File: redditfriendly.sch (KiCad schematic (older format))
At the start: 48 parts, among them J1 PJ-077, J2 Conn_01x06_Female, J3 Conn_01x02_Female, J4 Conn_01x06_Female, J5 Conn_01x04_Female, J6 Conn_01x6_Female, Q1 MMBT2222A-TP, Q2 MMBT2222A-TP, SW1 SW_Push, SW2 SW_Push, U1 ESP32-WROOM-32U, U2 LMR33620Simple, U3 TLC5971

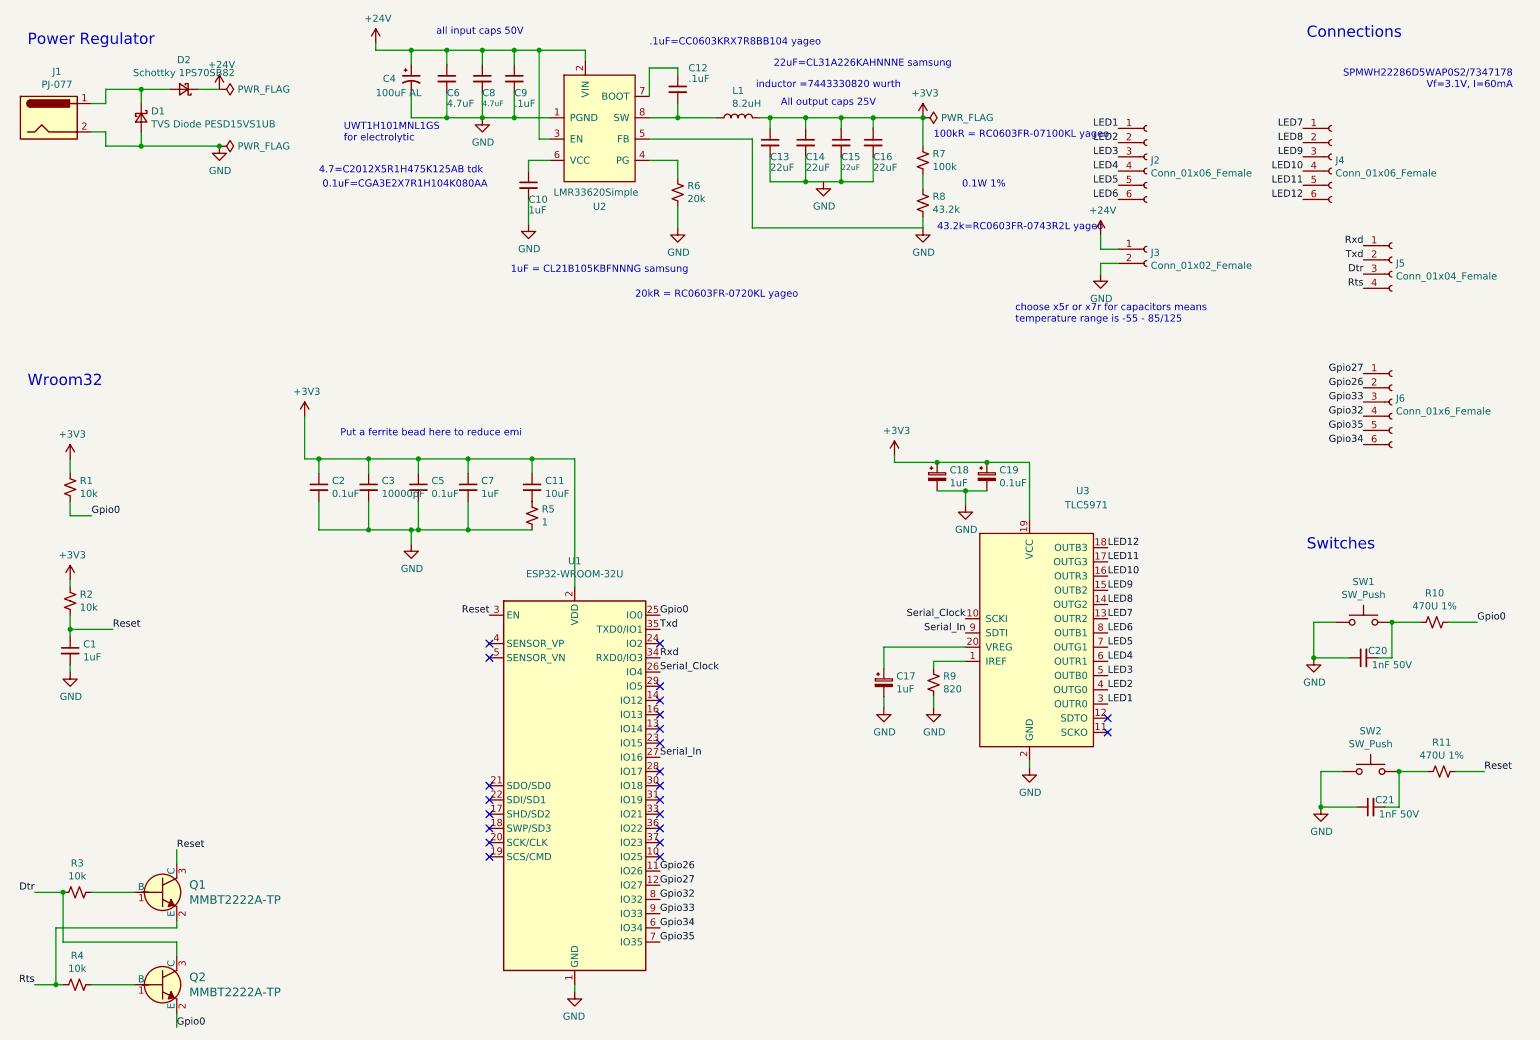
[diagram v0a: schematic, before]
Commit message: Created pmic footprint
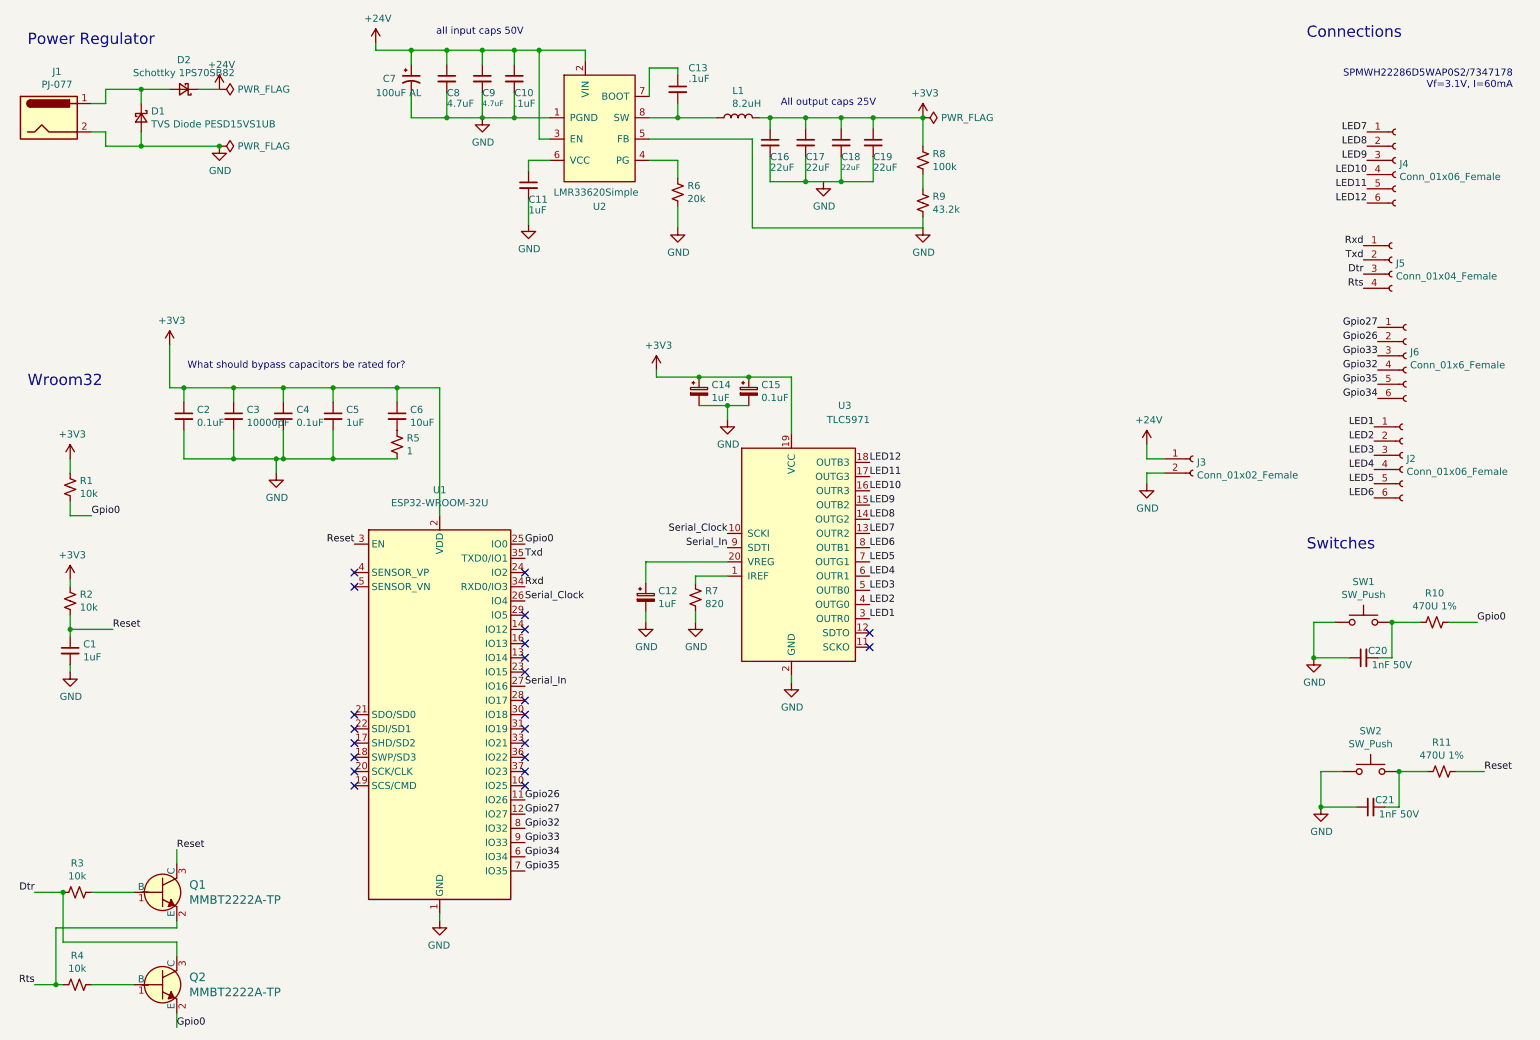
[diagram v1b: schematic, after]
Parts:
- C7: renamed from C4; footprint Capacitor_SMD:CP_Elec_6.3x5.4 -> (none)
- L1: footprint Keith:wurth 7443330820 8.2uH -> keith:Wurth 74437349012 Inductor
- U2: footprint Keith:lmr33620HSOIC -> (none)
- renumbered C9 to C10, C10 to C11, C17 to C12, C12 to C13, C18 to C14, C19 to C15, C13 to C16, C14 to C17, C15 to C18, C16 to C19, C5 to C4, C7 to C5, C11 to C6, C6 to C8, C8 to C9, R9 to R7, R7 to R8, R8 to R9
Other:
- note added: "What should bypass capacitors be rated for?"
- note removed: ".1uF=CC0603KRX7R8BB104 yageo"
- note removed: "0.1W 1%"
- note removed: "0.1uF=CGA3E2X7R1H104K080AA"
- note removed: "100kR = RC0603FR-07100KL yageo"
- note removed: "1uF = CL21B105KBFNNNG samsung"
- note removed: "20kR = RC0603FR-0720KL yageo"
- note removed: "22uF=CL31A226KAHNNNE samsung"
- note removed: "4.7=C2012X5R1H475K125AB tdk"
- note removed: "43.2k=RC0603FR-0743R2L yageo"
- note removed: "Put a ferrite bead here to reduce emi"
- note removed: "UWT1H101MNL1GS\nfor electrolytic"
- note removed: "choose x5r or x7r for capacitors means \ntemperature range is -55 - 85/125"
- note removed: "inductor =7443330820 wurth"
- moved on the sheet: C12, C14, C15, C2, C3, C4, C5, C6, J2, J3, J4, J6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
